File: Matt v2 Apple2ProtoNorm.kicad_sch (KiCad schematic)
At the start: 5 parts, among them M1 Fan_Tacho_PWM, M2 M

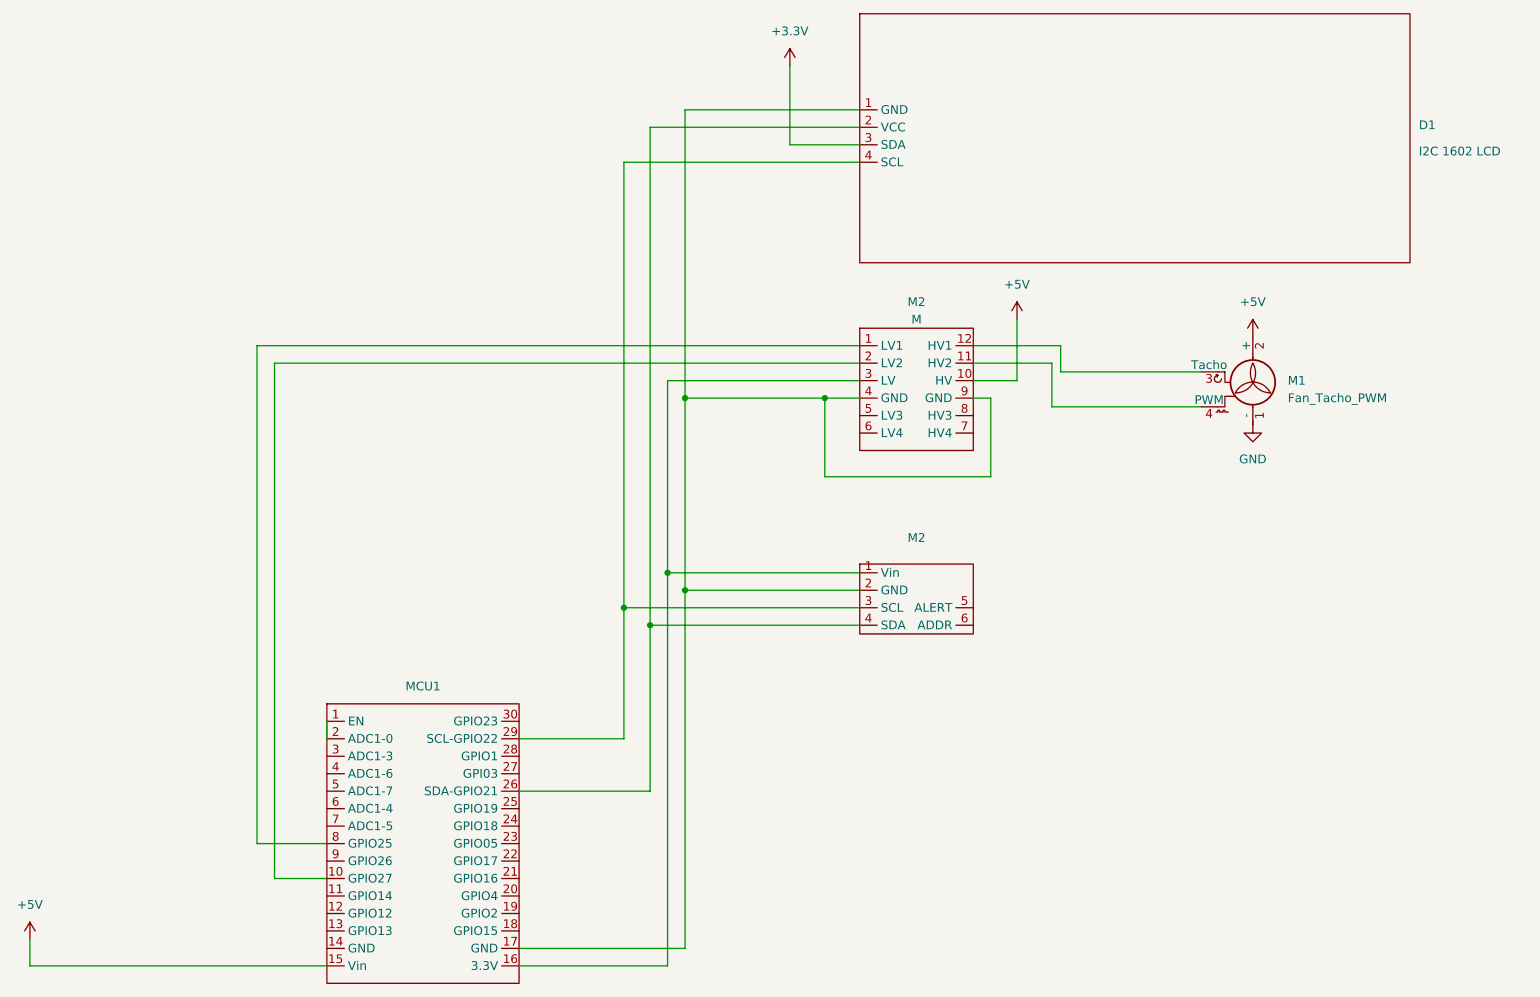
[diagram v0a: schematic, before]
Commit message: Add diode and change display to 5v power
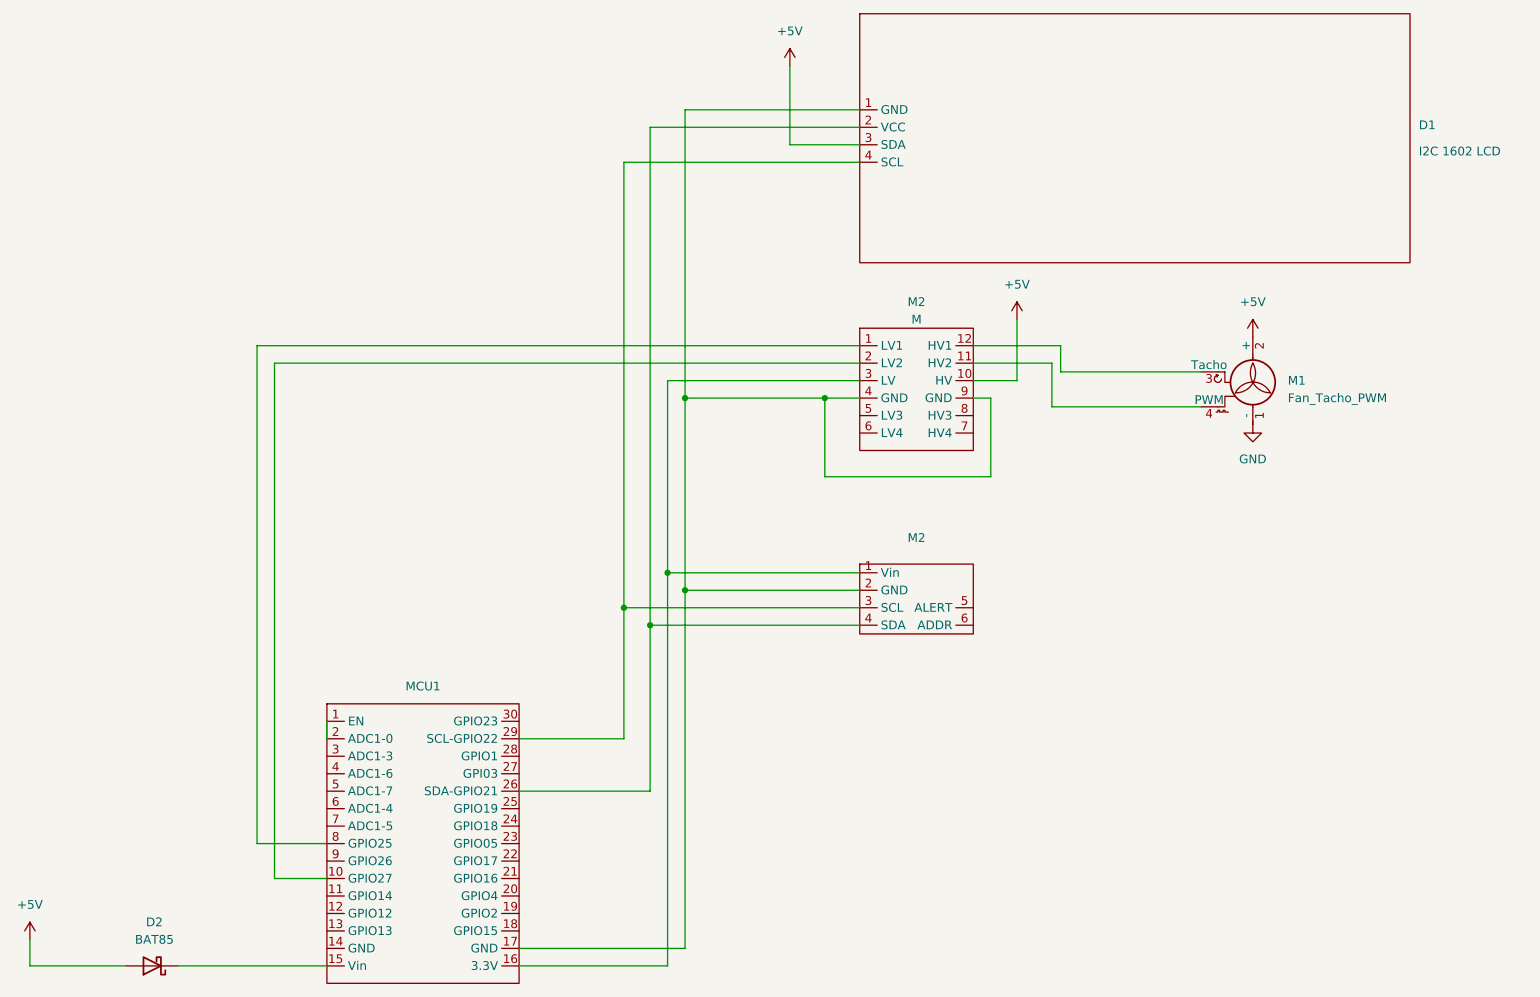
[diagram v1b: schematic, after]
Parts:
- added D2: BAT85, Diode_THT:D_DO-35_SOD27_P7.62mm_Horizontal, symbol Diode:BAT85
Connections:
- net +3.3V is gone; now on net +5V: D1.3 (SDA)
- net +5V: now also D2.2 (A); no longer MCU1.15 (Vin)
- new net: D2.1 (K), MCU1.15 (Vin)

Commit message: updates
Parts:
- added R1: 4700, symbol Device:R
- added R2: 5600, symbol Device:R
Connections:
- net +5V: now also D1.2 (VCC), M2.1 (Vin), R1.1; no longer D1.3 (SDA)
- net GND: now also R2.2
- net at M2.3 (LV), MCU1.16 (3.3V): no longer M2.1 (Vin)
- net at M2.4 (SDA), MCU1.26 (SDA-GPIO21): now also D1.3 (SDA); no longer D1.2 (VCC)
- net at MCU1.1 (EN), MCU1.2 (ADC1-0): now also R1.2, R2.1
